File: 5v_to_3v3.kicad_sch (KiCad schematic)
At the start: 14 parts, among them U3 ST1S12GR

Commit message: commit before updating to LiveAstra lib
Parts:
- C12, C15: now left out of the parts list
- L1: value 4u7 -> 4u7H
- L2: value 22u -> 22uH
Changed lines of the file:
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@@
 		(unit 1)
 		(exclude_from_sim no)
-		(in_bom yes)
+		(in_bom no)
 		(on_board yes)
 		(dnp yes)
@@
 		(unit 1)
 		(exclude_from_sim no)
-		(in_bom yes)
+		(in_bom no)
 		(on_board yes)
 		(dnp yes)
@@
 			)
 		)
-		(property "Value" "22u"
+		(property "Value" "22uH"
 			(at 213.36 96.52 0)
 			(effects
@@
 			)
 		)
-		(property "Value" "4u7"
+		(property "Value" "4u7H"
 			(at 106.68 96.52 0)
 			(effects

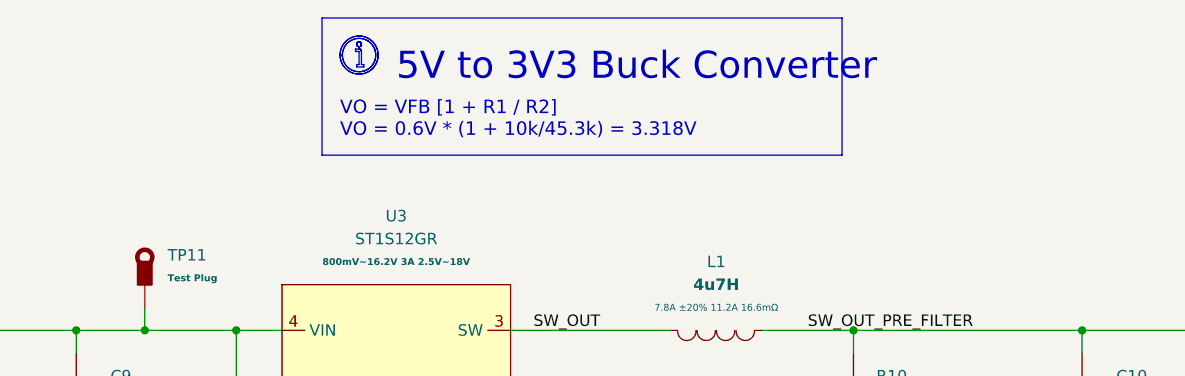
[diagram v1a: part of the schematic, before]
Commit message: Updated library name, updated and verified all footprints
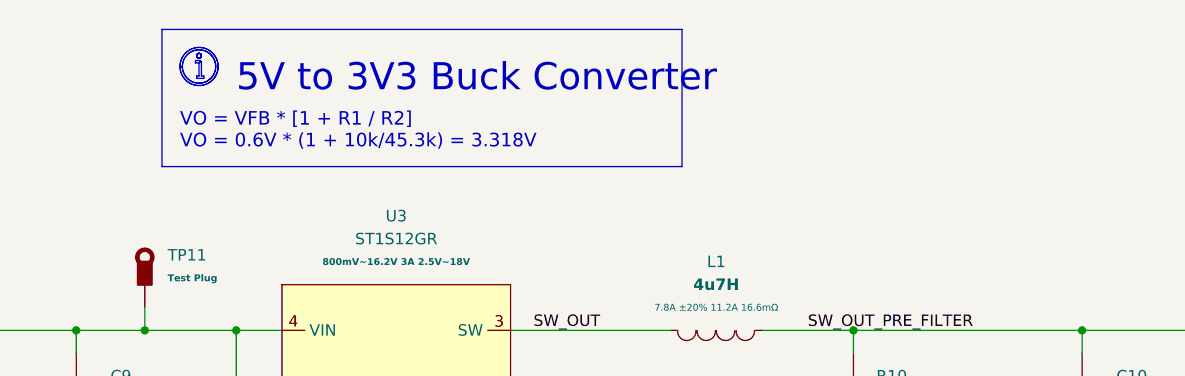
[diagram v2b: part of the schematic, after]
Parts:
- C10, C11, C9: symbol EASYEDA2KICAD:C_4u7_X5R_0603 -> LiveAstra:C_4u7_X5R_0603
- C12, C15: symbol EASYEDA2KICAD:C_47u_X5R_0805 -> LiveAstra:C_47u_X5R_0805; now in the parts list
- C13: symbol EASYEDA2KICAD:C_22uF_X5R_0603 -> LiveAstra:C_22uF_X5R_0603
- C14: symbol EASYEDA2KICAD:C_47u_X5R_0805 -> LiveAstra:C_47u_X5R_0805
- L1: footprint EASYEDA2KICAD:IND-SMD_L7.5-W7.0_SPM7054VT-330M-D -> LiveAstra:IND-SMD_L7.5-W7.0_SPM7054VT-330M-D; symbol EASYEDA2KICAD:L_4u7_7.8A_SPM7054VT-4R7M-D -> LiveAstra:L_4u7_7.8A_SPM7054VT-4R7M-D
- L2: footprint EASYEDA2KICAD:IND-SMD_L4.0-W4.0_SLW4010S -> LiveAstra:IND-SMD_L4.0-W4.0_SLW4010S; symbol EASYEDA2KICAD:L_22u_1A_ SWPA4030S220MT -> LiveAstra:L_22u_1A_ SWPA4030S220MT
- R10: symbol EASYEDA2KICAD:R_45k3Ohm_0402_62mW -> LiveAstra:R_45k3Ohm_0402_62mW
- R11: symbol EASYEDA2KICAD:R_10kOhm_0402_62mW -> LiveAstra:R_10kOhm_0402_62mW
- TP11, TP15: symbol EASYEDA2KICAD:TestPoint_Thimble -> LiveAstra:TestPoint_Thimble
- U3: footprint Package_TO_SOT_SMD:TSOT-23-5 -> LiveAstra:STEP_DOWN_ST1S12GR_TSOT-23-5; symbol EASYEDA2KICAD:DC_DC_Step_Down_Converter_ST1S12GR -> LiveAstra:DC_DC_Step_Down_Converter_ST1S12GR
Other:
- note added: "VO = VFB * [1 + R1 / R2] VO = 0.6V * (1 + 10k/45.3k) = 3.318V"
- note removed: "VO = VFB [1 + R1 / R2] VO = 0.6V * (1 + 10k/45.3k) = 3.318V"

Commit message: Finished layout no drc or erc errors
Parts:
- removed L1: 4u7H, LiveAstra:IND-SMD_L7.5-W7.0_SPM7054VT-330M-D, symbol LiveAstra:L_4u7_7.8A_SPM7054VT-4R7M-D
- removed L2: 22uH, LiveAstra:IND-SMD_L4.0-W4.0_SLW4010S, symbol LiveAstra:L_22u_1A_ SWPA4030S220MT
- added L1: 2u2H, LiveAstra:L_MDA4020_4.1x4.5mm, symbol LiveAstra:L_2u2H_4A_MDA4020-2R2M
- added L2: 22uH, LiveAstra:L_Sunlord_SWPA4030S, symbol LiveAstra:L_22uH_1A_ SWPA4030S220MT
- added R9: 1M, LiveAstra:R_0805_2012Metric_Pad1.20x1.40mm_HandSolder, symbol LiveAstra:R_1MOhm_0805_125mW
- added TP56: TestPoint_Thimble, LiveAstra:TestPoint_Loop_D3.50mm_Drill0.9mm_Beaded, symbol LiveAstra:TestPoint_Thimble
- C10, C11, C9: footprint Capacitor_SMD:C_0201_0603Metric -> LiveAstra:C_0603_1608Metric
- C12, C14, C15: footprint Capacitor_SMD:C_0805_2012Metric_Pad1.18x1.45mm_HandSolder -> LiveAstra:C_0805_2012Metric_Pad1.18x1.45mm_HandSolder
- C13: footprint Capacitor_SMD:C_0603_1608Metric -> LiveAstra:C_0603_1608Metric
- R10, R11: footprint Resistor_SMD:R_0402_1005Metric -> LiveAstra:R_0402_1005Metric
- TP10: renamed from TP15; footprint TestPoint:TestPoint_Loop_D3.50mm_Drill0.9mm_Beaded -> LiveAstra:TestPoint_Loop_D3.50mm_Drill0.9mm_Beaded; now not fitted; now left out of the parts list
- TP9: renamed from TP11; footprint TestPoint:TestPoint_Loop_D3.50mm_Drill0.9mm_Beaded -> LiveAstra:TestPoint_Loop_D3.50mm_Drill0.9mm_Beaded; now not fitted; now left out of the parts list
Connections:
- net 3V3: now also L2.2
- net 5V: now also R9.2; no longer U3.1 (EN)
- net SW_OUT: now also L1.1
- net SW_OUT_PRE_FILTER renamed SW_OUT_UNFILTERED
- net SW_OUT_UNFILTERED: now also L1.2, L2.1, TP56.1
- new net EN: R9.1, U3.1 (EN)
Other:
- note added: "Cutoff frequency: 8.76kHz Not really needed. Mostly for educational purposes."
- note removed: "Cutoff frequency: 8.76kHz"
- moved on the sheet: C14, C9

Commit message: Work on kibot
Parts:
- C12, C14, C15: Extra Values 6.3V X5R ±20% 0805 -> 6.3V X5R ±20% 0805

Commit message: workflow
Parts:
- TP10, TP56, TP9: now fitted
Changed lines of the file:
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@@
+			)
+		)
+		(property "Extra Value" ""
+			(at 187.96 129.54 0)
+			(effects
+				(font
+					(size 1.27 1.27)
+				)
+				(hide yes)
 			)
 		)
@@
 			)
 		)
+		(property "Extra Value" ""
+			(at 213.36 101.6 0)
+			(effects
+				(font
+					(size 1.27 1.27)
+				)
+				(hide yes)
+			)
+		)
 		(pin "1"
 		)
@@
 			)
 		)
+		(property "Extra Value" ""
+			(at 48.26 116.84 0)
+			(effects
+				(font
+					(size 1.27 1.27)
+				)
+				(hide yes)
+			)
+		)
 		(pin "2"
 		)
@@
 			)
 		)
+		(property "Extra Value" ""
+			(at 147.32 109.22 0)
+			(effects
+				(font
+					(size 1.27 1.27)
+				)
+				(hide yes)
+			)
+		)
 		(pin "2"
 		)
@@
 			)
 		)
+		(property "Extra Value" ""
+			(at 198.12 109.22 0)
+			(effects
+				(font
+					(size 1.27 1.27)
+				)
+				(hide yes)
+			)
+		)
 		(pin "1"
 		)
@@
 			)
 		)
+		(property "Extra Value" ""
+			(at 248.92 129.54 0)
+			(effects
+				(font
+					(size 1.27 1.27)
+				)
+				(hide yes)
+			)
+		)
 		(pin "1"
 		)
@@
 		(in_bom no)
 		(on_board yes)
-		(dnp yes)
+		(dnp no)
 		(fields_autoplaced yes)
 		(property "Reference" "TP10"
@@
 			)
 		)
+		(property "Extra Value" ""
+			(at 254 99.06 0)
+			(effects
+				(font
+					(size 1.27 1.27)
+				)
+				(hide yes)
+			)
+		)
 		(pin "1"
 		)
@@
 			)
 		)
+		(property "Extra Value" ""
+			(at 121.92 124.46 0)
+			(effects
+				(font
+					(size 1.27 1.27)
+				)
+				(hide yes)
+			)
+		)
 		(pin "1"
 		)
@@
 			)
 		)
+		(property "Extra Value" ""
+			(at 228.6 109.22 0)
+			(effects
+				(font
+					(size 1.27 1.27)
+				)
+				(hide yes)
+			)
+		)
 		(pin "1"
 		)
@@
 			)
 		)
+		(property "Extra Value" ""
+			(at 121.92 109.22 0)
+			(effects
+				(font
+					(size 1.27 1.27)
+				)
+				(hide yes)
+			)
+		)
 		(pin "1"
 		)
@@
 			)
 		)
+		(property "Extra Value" ""
+			(at 71.12 109.22 0)
+			(effects
+				(font
+					(size 1.27 1.27)
+				)
+				(hide yes)
+			)
+		)
 		(pin "2"
 		)
@@
 		(in_bom no)
 		(on_board yes)
-		(dnp yes)
+		(dnp no)
 		(fields_autoplaced yes)
 		(property "Reference" "TP56"
@@
 			)
 		)
+		(property "Extra Value" ""
+			(at 177.8 99.06 0)
+			(effects
+				(font
+					(size 1.27 1.27)
+				)
+				(hide yes)
+			)
+		)
 		(pin "1"
 		)
@@
 			)
 		)
+		(property "Extra Value" ""
+			(at 27.94 124.46 0)
+			(effects
+				(font
+					(size 1.27 1.27)
+				)
+				(hide yes)
+			)
+		)
 		(pin "2"
 		)
@@
 		(in_bom no)
 		(on_board yes)
-		(dnp yes)
+		(dnp no)
 		(fields_autoplaced yes)
 		(property "Reference" "TP9"
@@
 			)
 		)
+		(property "Extra Value" ""
+			(at 48.26 99.06 0)
+			(effects
+				(font
+					(size 1.27 1.27)
+				)
+				(hide yes)
+			)
+		)
 		(pin "1"
 		)
@@
 			)
 		)
+		(property "Extra Value" ""
+			(at 106.68 101.6 0)
+			(effects
+				(font
+					(size 1.27 1.27)
+				)
+				(hide yes)
+			)
+		)
 		(pin "1"
 		)
@@
 			)
 		)
+		(property "Extra Value" ""
+			(at 167.64 109.22 0)
+			(effects
+				(font
+					(size 1.27 1.27)
+				)
+				(hide yes)
+			)
+		)

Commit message: workflow
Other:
- title: (none) -> 5V to 3V3
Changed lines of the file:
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@@
 	(generator_version "8.0")
 	(paper "A4")
+	(title_block
+		(title "5V to 3V3")
+	)
 	(junction
 		(at 198.12 101.6)
